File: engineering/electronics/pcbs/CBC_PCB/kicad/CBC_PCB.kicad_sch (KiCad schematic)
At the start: 0 parts

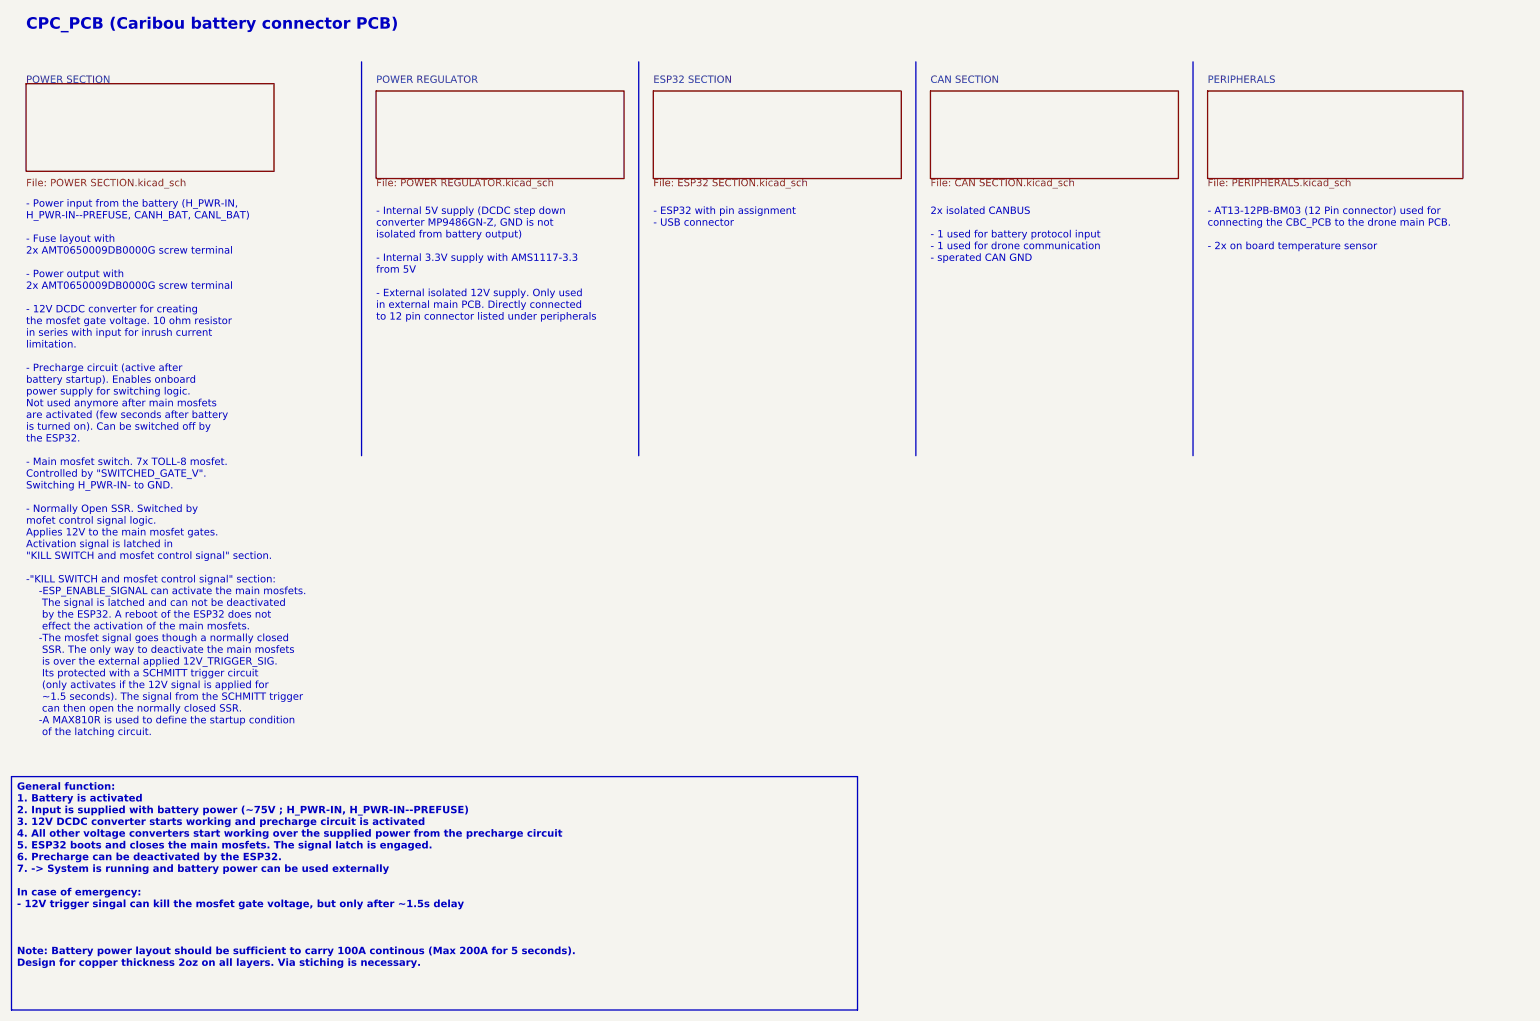
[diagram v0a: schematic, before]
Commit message: fix(cbc): integrate ordered PCB update
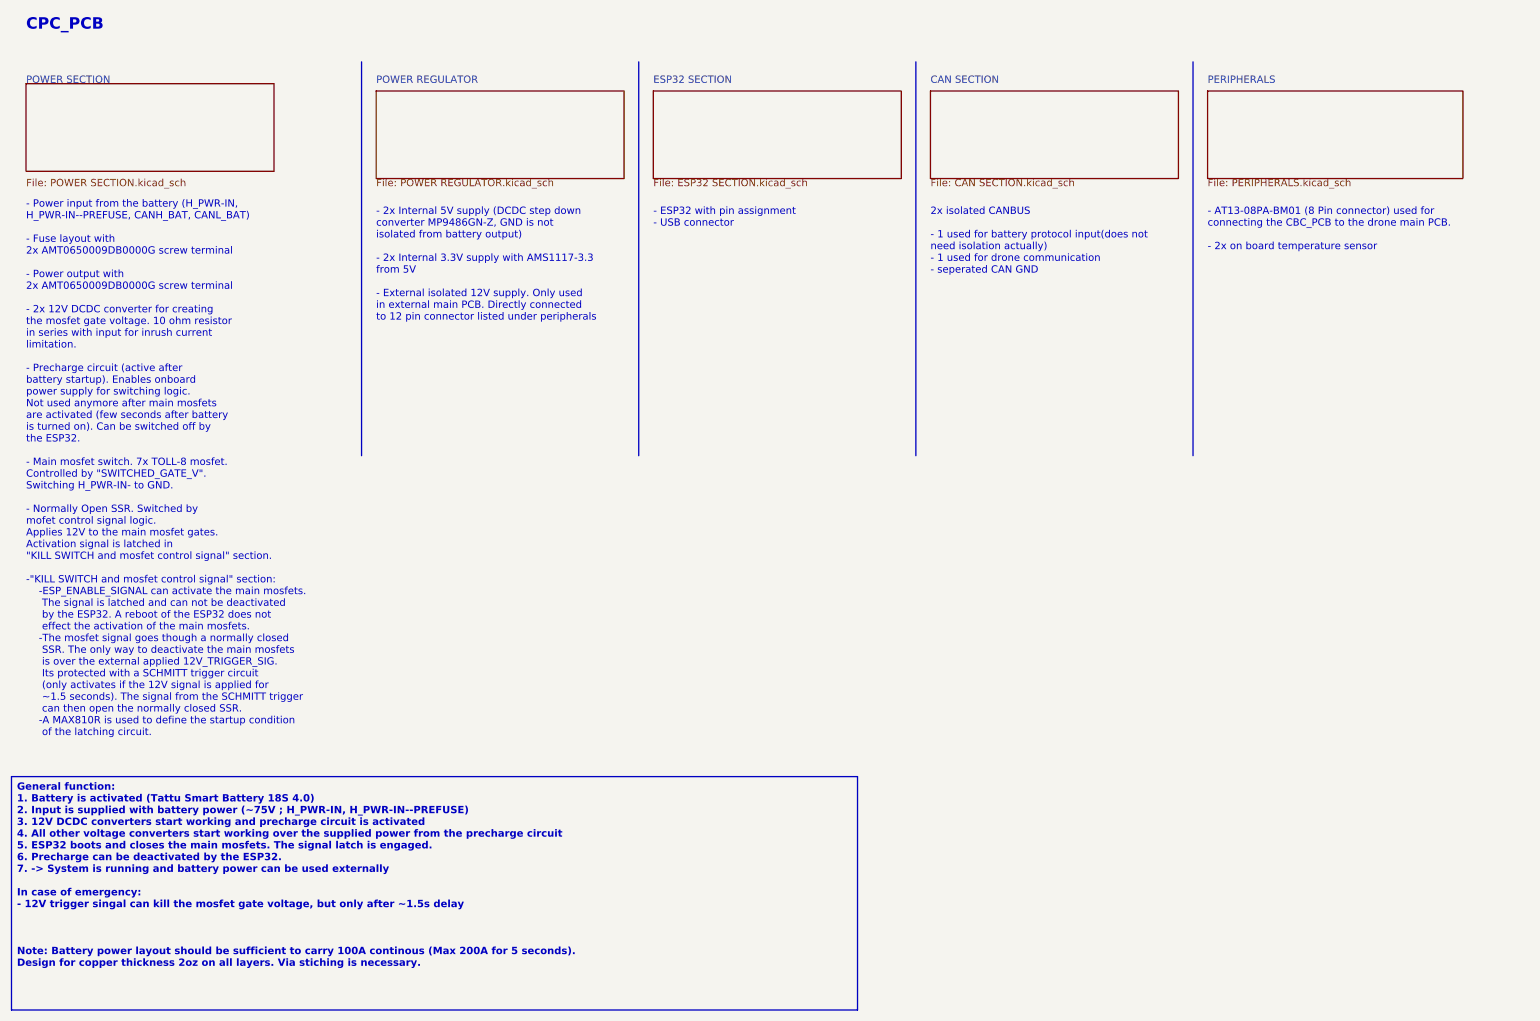
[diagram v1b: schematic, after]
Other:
- note added: "- 2x Internal 5V supply (DCDC step down converter MP9486GN-Z, GND is not isolated from battery output) - 2x Internal 3.3V supply with AMS1117-3.3 from 5V - External isolated 12V supply. Only used in external main PCB. Directly connected to 12 pin connector listed under peripherals"
- note added: "- AT13-08PA-BM01 (8 Pin connector) used for connecting the CBC_PCB to the drone main PCB. - 2x on board temperature sensor"
- note added: "- Power input from the battery (H_PWR-IN, H_PWR-IN--PREFUSE, CANH_BAT, CANL_BAT) - Fuse layout with 2x AMT0650009DB0000G screw terminal - Power output with 2x AMT0650009DB0000G screw terminal - 2x 12V DCDC converter for creating the mosfet gate voltage. 10 ohm resistor in series with input for inrush current limitation. - Precharge circuit (active after battery startup). Enables onboard power sup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"
- note added: "2x isolated CANBUS - 1 used for battery protocol input(does not need isolation actually) - 1 used for drone communication - seperated CAN GND"
- note added: "CPC_PCB"
- note removed: "- AT13-12PB-BM03 (12 Pin connector) used for connecting the CBC_PCB to the drone main PCB. - 2x on board temperature sensor"
- note removed: "- Internal 5V supply (DCDC step down converter MP9486GN-Z, GND is not isolated from battery output) - Internal 3.3V supply with AMS1117-3.3 from 5V - External isolated 12V supply. Only used in external main PCB. Directly connected to 12 pin connector listed under peripherals"
- note removed: "- Power input from the battery (H_PWR-IN, H_PWR-IN--PREFUSE, CANH_BAT, CANL_BAT) - Fuse layout with 2x AMT0650009DB0000G screw terminal - Power output with 2x AMT0650009DB0000G screw terminal - 12V DCDC converter for creating the mosfet gate voltage. 10 ohm resistor in series with input for inrush current limitation. - Precharge circuit (active after battery startup). Enables onboard power supply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"
- note removed: "2x isolated CANBUS - 1 used for battery protocol input - 1 used for drone communication - sperated CAN GND"
- note removed: "CPC_PCB (Caribou battery connector PCB)"
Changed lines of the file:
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@@
 	(generator_version "10.0")
 	(paper "A4")
-	(text "- Internal 5V supply (DCDC step down\nconverter MP9486GN-Z, GND is not\nisolated from battery output)\n\n- Internal 3.3V supply with AMS1117-3.3\nfrom 5V\n\n- External isolated 12V supply. Only used\nin external main PCB. Directly connected\nto 12 pin connector listed under peripherals "
+	(text "- 2x Internal 5V supply (DCDC step down\nconverter MP9486GN-Z, GND is not\nisolated from battery output)\n\n- 2x Internal 3.3V supply with AMS1117-3.3\nfrom 5V\n\n- External isolated 12V supply. Only used\nin external main PCB. Directly connected\nto 12 pin connector listed under peripherals "
 		(exclude_from_sim no)
 		(at 86.36 50.8 0)
@@
 		)
 	)
-	(text "CPC_PCB (Caribou battery connector PCB)"
+	(text "CPC_PCB"
 		(exclude_from_sim no)
 		(at 25.4 17.78 0)
@@
 		)
 	)
-	(text "- Power input from the battery (H_PWR-IN,\nH_PWR-IN--PREFUSE, CANH_BAT, CANL_BAT)\n\n- Fuse layout with\n2x AMT0650009DB0000G screw terminal\n\n- Power output with\n2x AMT0650009DB0000G screw terminal\n\n- 12V DCDC converter for creating\nthe mosfet gate voltage. 10 ohm resistor\nin series with input for inrush current\nlimitation.\n\n- Precharge circuit (active after\nbattery startup). Enables onboard\npower supply for switching logic.\nNot used anymore after main mosfets\nare activated (few seconds after battery\nis turned on). Can be switched off by\nthe ESP32.\n\n- Main mosfet switch. 7x TOLL-8 mosfet.\nControlled by \"SWITCHED_GATE_V\".\nSwitching H_PWR-IN- to GND.\n\n- Normally Open SSR. Switched by\nmofet control signal logic.\nApplies 12V to the main mosfet gates.\nActivation signal is latched in\n\"KILL SWITCH and mosfet control signal\" section.\n\n-\"KILL SWITCH and mosfet control signal\" section:\n	-ESP_ENABLE_SIGNAL can activate the main mosfets.\n	 The signal is latched and can not be deactivated\n	 by the ESP32. A reboot of the ESP32 does not\n	 effect the activation of the main mosfets.\n	-The mosfet signal goes though a normally closed\n	 SSR. The only way to deactivate the main mosfets\n	 is over the external applied 12V_TRIGGER_SIG.\n	 Its protected with a SCHMITT trigger circuit\n	 (only activates if the 12V signal is applied for\n	 ~1.5 seconds). The signal from the SCHMITT trigger\n	 can then open the normally closed SSR.\n	-A MAX810R is used to define the startup condition\n	 of the latching circuit.\n\n"
+	(text "- Power input from the battery (H_PWR-IN,\nH_PWR-IN--PREFUSE, CANH_BAT, CANL_BAT)\n\n- Fuse layout with\n2x AMT0650009DB0000G screw terminal\n\n- Power output with\n2x AMT0650009DB0000G screw terminal\n\n- 2x 12V DCDC converter for creating\nthe mosfet gate voltage. 10 ohm resistor\nin series with input for inrush current\nlimitation.\n\n- Precharge circuit (active after\nbattery startup). Enables onboard\npower supply for switching logic.\nNot used anymore after main mosfets\nare activated (few seconds after battery\nis turned on). Can be switched off by\nthe ESP32.\n\n- Main mosfet switch. 7x TOLL-8 mosfet.\nControlled by \"SWITCHED_GATE_V\".\nSwitching H_PWR-IN- to GND.\n\n- Normally Open SSR. Switched by\nmofet control signal logic.\nApplies 12V to the main mosfet gates.\nActivation signal is latched in\n\"KILL SWITCH and mosfet control signal\" section.\n\n-\"KILL SWITCH and mosfet control signal\" section:\n	-ESP_ENABLE_SIGNAL can activate the main mosfets.\n	 The signal is latched and can not be deactivated\n	 by the ESP32. A reboot of the ESP32 does not\n	 effect the activation of the main mosfets.\n	-The mosfet signal goes though a normally closed\n	 SSR. The only way to deactivate the main mosfets\n	 is over the external applied 12V_TRIGGER_SIG.\n	 Its protected with a SCHMITT trigger circuit\n	 (only activates if the 12V signal is applied for\n	 ~1.5 seconds). The signal from the SCHMITT trigger\n	 can then open the normally closed SSR.\n	-A MAX810R is used to define the startup condition\n	 of the latching circuit.\n\n"
 		(exclude_from_sim no)
 		(at 25.4 49.53 0)
@@
 		)
 	)
-	(text "- AT13-12PB-BM03 (12 Pin connector) used for\nconnecting the CBC_PCB to the drone main PCB.\n\n- 2x on board temperature sensor"
+	(text "- AT13-08PA-BM01 (8 Pin connector) used for\nconnecting the CBC_PCB to the drone main PCB.\n\n- 2x on board temperature sensor"
 		(exclude_from_sim no)
 		(at 231.14 50.8 0)
@@
 		)
 	)
-	(text "2x isolated CANBUS\n\n- 1 used for battery protocol input\n- 1 used for drone communication\n- sperated CAN GND"
+	(text "2x isolated CANBUS\n\n- 1 used for battery protocol input(does not\nneed isolation actually)\n- 1 used for drone communication\n- seperated CAN GND"
 		(exclude_from_sim no)
 		(at 182.88 50.8 0)
@@
 		)
 	)
-	(text_box "General function:\n1. Battery is activated\n2. Input is supplied with battery power (~75V ; H_PWR-IN, H_PWR-IN--PREFUSE)\n3. 12V DCDC converter starts working and precharge circuit is activated\n4. All other voltage converters start working over the supplied power from the precharge circuit\n5. ESP32 boots and closes the main mosfets. The signal latch is engaged.\n6. Precharge can be deactivated by the ESP32.\n7. -> System is running and battery power can be used externally\n\nIn case of emergency:\n- 12V trigger singal can kill the mosfet gate voltage, but only after ~1.5s delay\n\n\n\nNote: Battery power layout should be sufficient to carry 100A continous (Max 200A for 5 seconds).\n      Design for copper thickness 2oz on all layers. Via stiching is necessary."
+	(text_box "General function:\n1. Battery is activated (Tattu Smart Battery 18S 4.0)\n2. Input is supplied with battery power (~75V ; H_PWR-IN, H_PWR-IN--PREFUSE)\n3. 12V DCDC converters start working and precharge circuit is activated\n4. All other voltage converters start working over the supplied power from the precharge circuit\n5. ESP32 boots and closes the main mosfets. The signal latch is engaged.\n6. Precharge can be deactivated by the ESP32.\n7. -> System is running and battery power can be used externally\n\nIn case of emergency:\n- 12V trigger singal can kill the mosfet gate voltage, but only after ~1.5s delay\n\n\n\nNote: Battery power layout should be sufficient to carry 100A continous (Max 200A for 5 seconds).\n      Design for copper thickness 2oz on all layers. Via stiching is necessary."
 		(exclude_from_sim no)
 		(at 22.86 149.86 0)
